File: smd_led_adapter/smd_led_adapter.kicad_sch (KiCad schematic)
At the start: 14 parts, among them J1 Conn_01x08_Male, J2 Conn_01x08_Male

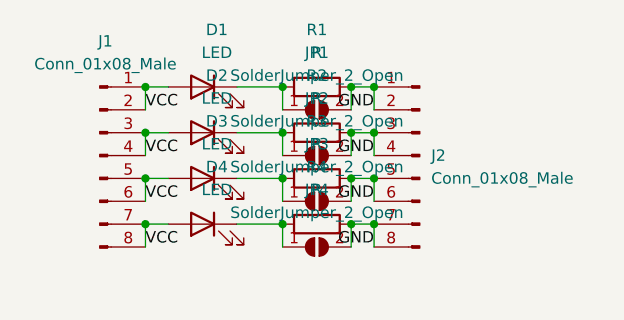
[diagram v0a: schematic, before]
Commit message: Make smd led adaptor cathode/anode commonable.
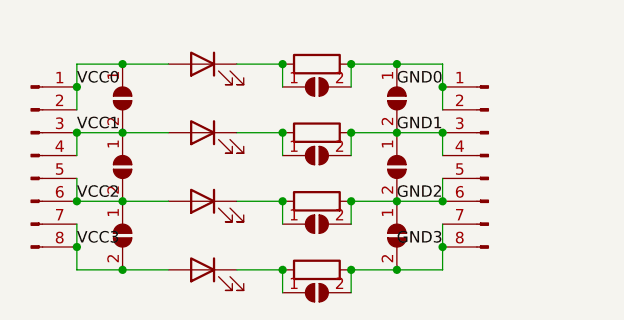
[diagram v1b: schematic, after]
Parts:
- added JP1, JP10, JP2, JP3, JP8, JP9: SolderJumper_2_Open, Jumper:SolderJumper-2_P1.3mm_Open_RoundedPad1.0x1.5mm, symbol Jumper:SolderJumper_2_Open
- renumbered JP1 to JP4, JP2 to JP5, JP3 to JP6, JP4 to JP7
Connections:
- removed net GND: J2.1 (Pin_1), J2.2 (Pin_2), J2.3 (Pin_3), J2.4 (Pin_4), J2.5 (Pin_5), J2.6 (Pin_6), J2.7 (Pin_7), J2.8 (Pin_8), JP4.2 (B), JP5.2 (B), JP6.2 (B), JP7.2 (B), R1.2, R2.2, R3.2, R4.2
- removed net VCC: D1.2 (A), D2.2 (A), D3.2 (A), D4.2 (A), J1.1 (Pin_1), J1.2 (Pin_2), J1.3 (Pin_3), J1.4 (Pin_4), J1.5 (Pin_5), J1.6 (Pin_6), J1.7 (Pin_7), J1.8 (Pin_8)
- new net GND0: J2.1 (Pin_1), J2.2 (Pin_2), JP4.2 (B), JP8.1 (A), R1.2
- new net GND1: J2.3 (Pin_3), J2.4 (Pin_4), JP5.2 (B), JP8.2 (B), JP9.1 (A), R2.2
- new net GND2: J2.5 (Pin_5), J2.6 (Pin_6), JP10.1 (A), JP6.2 (B), JP9.2 (B), R3.2
- new net GND3: J2.7 (Pin_7), J2.8 (Pin_8), JP10.2 (B), JP7.2 (B), R4.2
- new net VCC0: D1.2 (A), J1.1 (Pin_1), J1.2 (Pin_2), JP1.1 (A)
- new net VCC1: D2.2 (A), J1.3 (Pin_3), J1.4 (Pin_4), JP1.2 (B), JP2.1 (A)
- new net VCC2: D3.2 (A), J1.5 (Pin_5), J1.6 (Pin_6), JP2.2 (B), JP3.1 (A)
- new net VCC3: D4.2 (A), J1.7 (Pin_7), J1.8 (Pin_8), JP3.2 (B)
